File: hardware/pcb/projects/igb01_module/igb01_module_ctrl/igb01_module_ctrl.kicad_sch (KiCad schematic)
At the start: 297 parts, among them J1 ST_JACK_MIDI_OUT, J10 JACK_MAIN_L_OUT, J11 JACK_MAIN_R_OUT, J12 ST_JACK_MIDI_IN, J13 JACK_RST_OUT, J14 JACK_CV2_IN, J15 JACK_CV2_OUT, J16 JACK_CV4_OUT, J17 JACK_CV2_OUT, J18 JACK_CV4_OUT, J19 JACK_RTN_L_IN, J2 JACK_CLK_OUT, J20 JACK_RTN_R_IN, J21 JACK_SND_L_OUT, J22 JACK_SND_R_OUT, J23 TYPE_SELECT, J24 LEFT_CON, J25 RIGHT_CON, J26 TYPE_SELECT, J27 SWD_CON, J28 DISP_CON1, J29 Micro_SD_Card, J3 JACK_CV1_IN, J30 Conn_01x03, J31 Conn_01x03, J32 Conn_01x03, J33 POWER_CON, J4 JACK_CV1_OUT, J5 JACK_CV3_OUT, J6 JACK_CV1_OUT, J7 JACK_CV3_OUT, J8 JACK_EXT_L_IN, J9 JACK_EXT_R_IN, SW1 SW_Push_45deg, SW10 SW_Push_45deg, SW11 SW_Push_45deg, SW12 SW_Push_45deg, SW13 SW_Push_45deg, SW14 SW_Push_45deg, SW15 SW_Push_45deg, SW16 SW_Push_45deg, SW17 SW_Push_45deg, SW18 SW_Push_45deg, SW19 SW_Push_45deg, SW2 SW_Push_45deg, SW20 SW_Push_45deg, SW21 SW_Push_45deg, SW22 SW_Push_45deg, SW23 SW_Push_45deg, SW24 SW_Push_45deg, SW25 SW_Push_45deg, SW26 SW_Push_45deg, SW27 SW_Push_45deg, SW28 SW_Push_45deg, SW29 SW_Push_45deg, SW3 SW_Push_45deg, SW30 SW_Push_45deg, SW31 SW_Push_45deg, SW32 SW_Push_45deg, SW33 SW_Push_45deg, SW34 SW_Push_45deg, SW35 SW_Push_45deg, SW36 SW_Push_45deg, SW4 SW_Push_45deg, SW5 SW_Push_45deg, SW6 SW_Push_45deg, SW7 SW_Push_45deg, SW8 SW_Push_45deg, SW9 SW_Push_45deg, U1 TL074, U10 STM32G431RBTx, U11 TL074, U12 R-78B5.0-2.0, U13 LDK320-3.3V, U14 LDK320-3.3V, U15 LM4040DBZ-10, U2 TL074, U3 74AHCT1G125, U4 TLP2361, U5 74AHCT1G125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

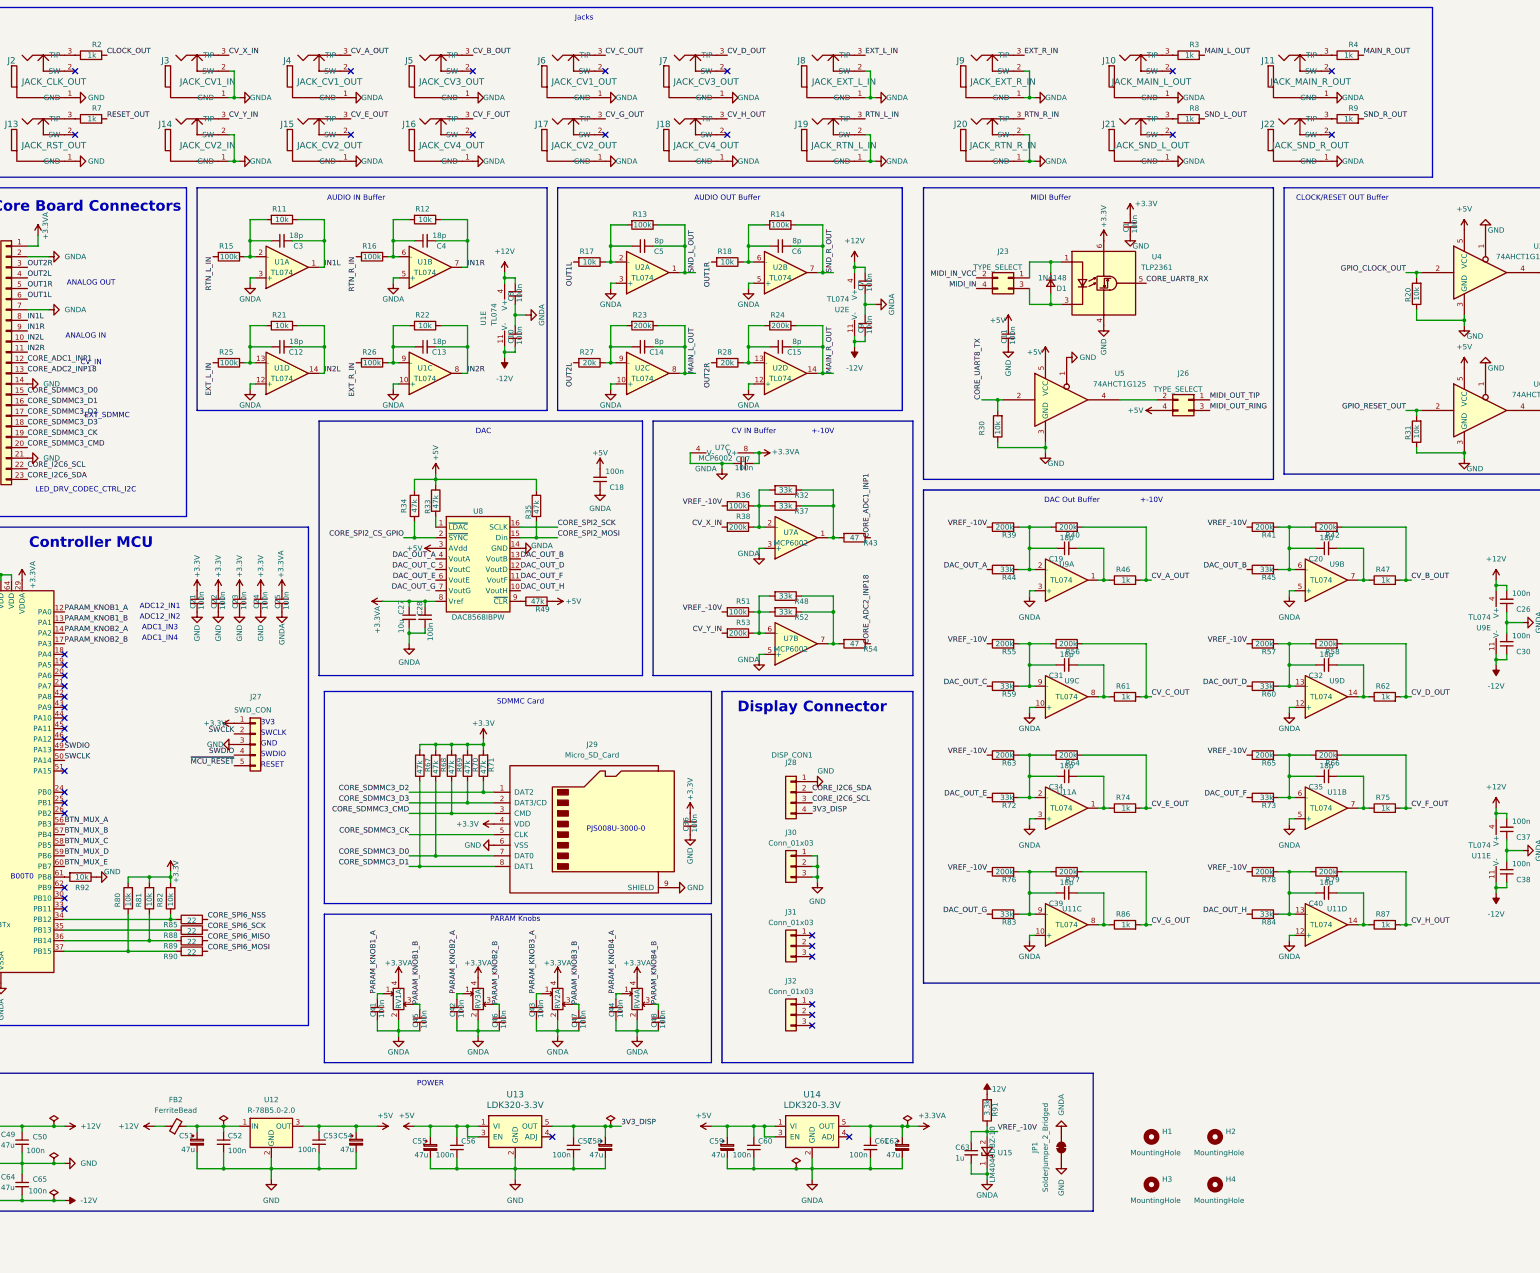
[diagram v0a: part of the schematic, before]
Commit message: update igb01 module control board
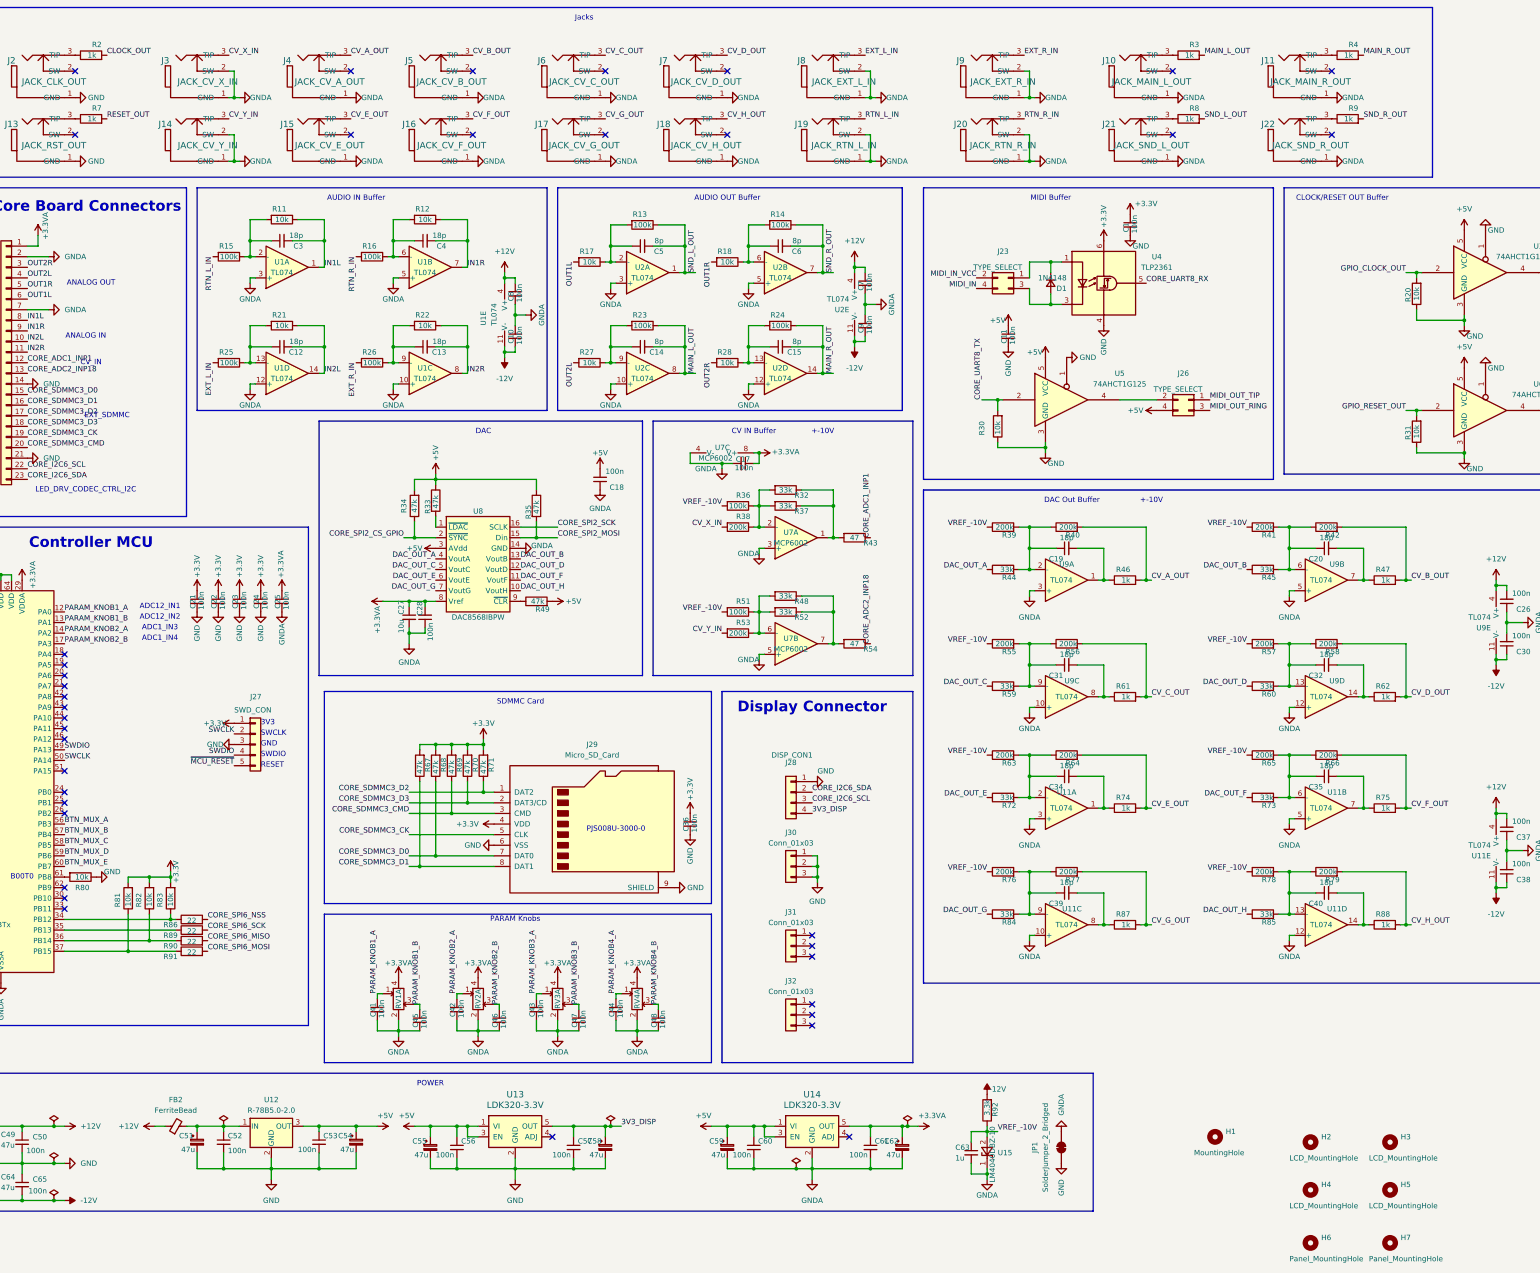
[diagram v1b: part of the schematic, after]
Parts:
- removed H1: MountingHole, MountingHole:MountingHole_3.2mm_M3, symbol Mechanical:MountingHole
- added H2, H5: LCD_MountingHole, MountingHole:MountingHole_2.2mm_M2, symbol Mechanical:MountingHole
- added H6, H7: Panel_MountingHole, MountingHole:MountingHole_3.2mm_M3, symbol Mechanical:MountingHole
- H3, H4: value MountingHole -> LCD_MountingHole; footprint MountingHole:MountingHole_3.2mm_M3 -> MountingHole:MountingHole_2.2mm_M2
- J14: value JACK_CV2_IN -> JACK_CV_Y_IN
- J15: value JACK_CV2_OUT -> JACK_CV_E_OUT
- J16: value JACK_CV4_OUT -> JACK_CV_F_OUT
- J17: value JACK_CV2_OUT -> JACK_CV_G_OUT
- J18: value JACK_CV4_OUT -> JACK_CV_H_OUT
- J3: value JACK_CV1_IN -> JACK_CV_X_IN
- J4: value JACK_CV1_OUT -> JACK_CV_A_OUT
- J5: value JACK_CV3_OUT -> JACK_CV_B_OUT
- J6: value JACK_CV1_OUT -> JACK_CV_C_OUT
- J7: value JACK_CV3_OUT -> JACK_CV_D_OUT
- R23, R24: value 200k -> 100k
- R27, R28: value 20k -> 10k
- renumbered C43 to C42, C42 to C43, C47 to C46, C46 to C47, H2 to H1, R92 to R80, R80 to R81, R81 to R82, R82 to R83, R83 to R84, R84 to R85, R85 to R86, R86 to R87, R87 to R88, R88 to R89, R89 to R90, R90 to R91, R91 to R92
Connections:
- net PARAM_KNOB2_A: now also C42.1, RV2.1; no longer C43.1, RV3.1
- net PARAM_KNOB2_B: now also C46.1, RV2.3; no longer C47.1, RV3.3
- net PARAM_KNOB3_A: now also C43.1, RV3.1; no longer C42.1, RV2.1
- net PARAM_KNOB3_B: now also C47.1, RV3.3; no longer C46.1, RV2.3
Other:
- moved on the sheet: C42, C43, C46, C47, RV2A, RV3A

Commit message: update igb01 module control board
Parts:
- removed C41, C42, C43, C44, C45, C46, C47, C48: 100n, Capacitor_SMD:C_0603_1608Metric, symbol Device:C_Small
- removed R19, R29: 1k, Resistor_SMD:R_0603_1608Metric, symbol Device:R
- removed R32, R48: 33k, Resistor_SMD:R_0603_1608Metric, symbol Device:R
- added C26: 10u, Capacitor_SMD:C_0805_2012Metric, symbol Device:C_Small
- C28: renamed from C27; footprint Capacitor_SMD:C_1206_3216Metric -> Capacitor_SMD:C_0805_2012Metric
- C51: renamed from C58; value 47u -> 100u
- D1: footprint Diode_SMD:D_SOD-323_HandSoldering -> custom:SOD-123
- D10, D11, D12, D13, D14, D15, D16, D17, D18, D19, D2, D20, D21, D22, D23, D24, D25, D26, D27, D28, D29, D3, D30, D31, D32, D33, D34, D35, D36, D37, D38, D39, D4, D40, D41, D5, D6, D7, D8, D9: footprint Diode_SMD:D_SOD-323_HandSoldering -> Diode_SMD:D_SOD-523
- D42, D43: footprint Diode_SMD:D_SOD-123F -> custom:SOD-123
- R1, R10, R5, R6: footprint Resistor_SMD:R_0603_1608Metric -> Resistor_SMD:R_1206_3216Metric
- R2, R3, R4, R7, R8, R9: footprint Resistor_SMD:R_0603_1608Metric -> Resistor_SMD:R_0805_2012Metric
- R30: renamed from R33; footprint Resistor_SMD:R_0402_1005Metric -> Resistor_SMD:R_0603_1608Metric
- R32: renamed from R35; footprint Resistor_SMD:R_0402_1005Metric -> Resistor_SMD:R_0603_1608Metric
- R33: renamed from R36; value 100k -> 200k
- R36: renamed from R39; footprint Resistor_SMD:R_0402_1005Metric -> Resistor_SMD:R_0603_1608Metric
- R37: renamed from R40; footprint Resistor_SMD:R_0402_1005Metric -> Resistor_SMD:R_0603_1608Metric
- R38: renamed from R41; footprint Resistor_SMD:R_0402_1005Metric -> Resistor_SMD:R_0603_1608Metric
- R39: renamed from R42; footprint Resistor_SMD:R_0402_1005Metric -> Resistor_SMD:R_0603_1608Metric
- R41: renamed from R44; footprint Resistor_SMD:R_0402_1005Metric -> Resistor_SMD:R_0603_1608Metric
- R42: renamed from R45; footprint Resistor_SMD:R_0402_1005Metric -> Resistor_SMD:R_0603_1608Metric
- R43: renamed from R46; footprint Resistor_SMD:R_0402_1005Metric -> Resistor_SMD:R_0805_2012Metric
- R44: renamed from R47; footprint Resistor_SMD:R_0402_1005Metric -> Resistor_SMD:R_0805_2012Metric
- R45: renamed from R49; footprint Resistor_SMD:R_0402_1005Metric -> Resistor_SMD:R_0603_1608Metric
- R47: renamed from R51; value 100k -> 200k
- R51: renamed from R55; footprint Resistor_SMD:R_0402_1005Metric -> Resistor_SMD:R_0603_1608Metric
- R52: renamed from R56; footprint Resistor_SMD:R_0402_1005Metric -> Resistor_SMD:R_0603_1608Metric
- R53: renamed from R57; footprint Resistor_SMD:R_0402_1005Metric -> Resistor_SMD:R_0603_1608Metric
- R54: renamed from R58; footprint Resistor_SMD:R_0402_1005Metric -> Resistor_SMD:R_0603_1608Metric
- R55: renamed from R59; footprint Resistor_SMD:R_0402_1005Metric -> Resistor_SMD:R_0603_1608Metric
- R56: renamed from R60; footprint Resistor_SMD:R_0402_1005Metric -> Resistor_SMD:R_0603_1608Metric
- R57: renamed from R61; footprint Resistor_SMD:R_0402_1005Metric -> Resistor_SMD:R_0805_2012Metric
- R58: renamed from R62; footprint Resistor_SMD:R_0402_1005Metric -> Resistor_SMD:R_0805_2012Metric
- R59: renamed from R63; footprint Resistor_SMD:R_0402_1005Metric -> Resistor_SMD:R_0603_1608Metric
- R60: renamed from R64; footprint Resistor_SMD:R_0402_1005Metric -> Resistor_SMD:R_0603_1608Metric
- R61: renamed from R65; footprint Resistor_SMD:R_0402_1005Metric -> Resistor_SMD:R_0603_1608Metric
- R62: renamed from R66; footprint Resistor_SMD:R_0402_1005Metric -> Resistor_SMD:R_0603_1608Metric
- R68: renamed from R72; footprint Resistor_SMD:R_0402_1005Metric -> Resistor_SMD:R_0603_1608Metric
- R69: renamed from R73; footprint Resistor_SMD:R_0402_1005Metric -> Resistor_SMD:R_0603_1608Metric
- R70: renamed from R74; footprint Resistor_SMD:R_0402_1005Metric -> Resistor_SMD:R_0805_2012Metric
- R71: renamed from R75; footprint Resistor_SMD:R_0402_1005Metric -> Resistor_SMD:R_0805_2012Metric
- R72: renamed from R76; footprint Resistor_SMD:R_0402_1005Metric -> Resistor_SMD:R_0603_1608Metric
- R73: renamed from R77; footprint Resistor_SMD:R_0402_1005Metric -> Resistor_SMD:R_0603_1608Metric
- R74: renamed from R78; footprint Resistor_SMD:R_0402_1005Metric -> Resistor_SMD:R_0603_1608Metric
- R75: renamed from R79; footprint Resistor_SMD:R_0402_1005Metric -> Resistor_SMD:R_0603_1608Metric
- R80: renamed from R84; footprint Resistor_SMD:R_0402_1005Metric -> Resistor_SMD:R_0603_1608Metric
- R81: renamed from R85; footprint Resistor_SMD:R_0402_1005Metric -> Resistor_SMD:R_0603_1608Metric
- R83: renamed from R87; footprint Resistor_SMD:R_0402_1005Metric -> Resistor_SMD:R_0805_2012Metric
- R84: renamed from R88; footprint Resistor_SMD:R_0402_1005Metric -> Resistor_SMD:R_0805_2012Metric
- renumbered C26 to C27, C28 to C29, C29 to C30, C30 to C31, C31 to C32, C32 to C33, C33 to C34, C34 to C35, C35 to C36, C36 to C37, C37 to C38, C38 to C39, C39 to C40, C40 to C41, C49 to C42, C50 to C43, C51 to C44, C52 to C45, C53 to C46, C54 to C47, C55 to C48, C56 to C49, C57 to C50, C59 to C52, C60 to C53, C61 to C54, C62 to C55, C63 to C56, C64 to C57, C65 to C58, R20 to R19, R21 to R20, R22 to R21, R23 to R22, R24 to R23, R25 to R24, R26 to R25, R27 to R26, R28 to R27, R30 to R28, R31 to R29, R34 to R31, R37 to R34, R38 to R35, R43 to R40, R50 to R46, R52 to R48, R53 to R49, R54 to R50, R67 to R63, R68 to R64, R69 to R65, R70 to R66, R71 to R67, R80 to R76, R81 to R77, R82 to R78, R83 to R79, R86 to R82, R89 to R85, R90 to R86, R91 to R87, R92 to R88
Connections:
- net +3.3VA: now also C26.1
- net CLOCK_OUT: now also U3.4
- net CV_A_OUT: now also R54.2, R58.2; no longer R37.2, R43.2
- net CV_B_OUT: now also R37.2, R43.2; no longer R39.2, R44.2
- net CV_C_OUT: now also R75.2, R84.2; no longer R52.2, R57.2
- net CV_D_OUT: now also R60.2, R70.2; no longer R54.2, R58.2
- net CV_E_OUT: now also R52.2, R57.2; no longer R60.2, R70.2
- net CV_F_OUT: now also R39.2, R44.2; no longer R62.2, R71.2
- net CV_H_OUT: now also R62.2, R71.2; no longer R75.2, R84.2
- net GNDA: now also C26.2
- net RESET_OUT: now also U6.4

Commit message: update igb01 module control board: layout all nets
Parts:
- removed D2, D3, D4, D5, D6, D7, D8, D9: 1N4148, Diode_SMD:D_SOD-523, symbol Device:D_Small
- removed FB1, FB3: FerriteBead_Small, Resistor_SMD:R_1206_3216Metric, symbol Device:FerriteBead_Small
- removed FB2: FerriteBead, Resistor_SMD:R_1206_3216Metric, symbol Device:FerriteBead_Small
- removed J23, J26: TYPE_SELECT, Connector_PinSocket_2.54mm:PinSocket_2x02_P2.54mm_Vertical, symbol Connector_Generic:Conn_02x02_Odd_Even
- removed JP1: SolderJumper_2_Bridged, custom:GND_JUMPER_no_silk, symbol Jumper:SolderJumper_2_Bridged
- renumbered D18 to D10, D19 to D11, D20 to D12, D21 to D13, D22 to D14, D23 to D15, D24 to D16, D25 to D17, D26 to D18, D27 to D19, D10 to D2, D28 to D20, D29 to D21, D30 to D22, D31 to D23, D32 to D24, D33 to D25, D34 to D26, D35 to D27, D36 to D28, D37 to D29, D11 to D3, D38 to D30, D39 to D31, D40 to D32, D41 to D33, D42 to D34, D43 to D35, D12 to D4, D13 to D5, D14 to D6, D15 to D7, D16 to D8, D17 to D9
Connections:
- net GNDA is gone; now on net GND: C10.1, C16.2, C17.2, C18.1, C2.2, C25.2, C26.2, C27.1, C28.2, C29.1, C31.2, C38.1, C39.2, C52.2, C53.2, C54.2, C55.2, C56.2, C7.2, C8.2, C9.1, J10.1 (GND), J11.1 (GND), J14.1 (GND), J14.2 (SW), J15.1 (GND), J16.1 (GND), J17.1 (GND), J18.1 (GND), J19.1 (GND), J19.2 (SW), J20.1 (GND), J20.2 (SW), J21.1 (GND), J22.1 (GND), J25.2 (Pin_2), J25.7 (Pin_7), J3.1 (GND), J3.2 (SW), J4.1 (GND), J5.1 (GND), J6.1 (GND), J7.1 (GND), J8.1 (GND), J8.2 (SW), J9.1 (GND), J9.2 (SW), RV1.2, RV2.2, RV3.2, RV4.2, U1.10 (+), U1.12 (+), U1.3 (+), U1.5 (+), U10.27 (VSSA), U11.10 (+), U11.12 (+), U11.3 (+), U11.5 (+), U14.2 (GND), U15.1 (K), U2.10 (+), U2.12 (+), U2.3 (+), U2.5 (+), U7.3 (+), U7.4 (V-), U7.5 (+), U8.14 (GND), U9.10 (+), U9.12 (+), U9.3 (+), U9.5 (+)
- net MIDI_OUT_RING is gone; now on net +5V: R5.2
- net +12V: now also C44.1, C45.1, U12.1 (IN)
- net BTN_MUX_1: now also U10.26 (PB2); no longer SW1.2, U10.22 (PC4)
- net BTN_MUX_2: now also U10.25 (PB1); no longer SW2.2, U10.23 (PC5)
- net BTN_MUX_3: now also U10.24 (PB0); no longer SW3.2, U10.38 (PC6)
- net BTN_MUX_4: now also U10.23 (PC5); no longer SW4.2, U10.39 (PC7)
- net BTN_MUX_5: now also U10.22 (PC4); no longer SW5.2, U10.40 (PC8)
- net BTN_MUX_6: now also U10.21 (PA7); no longer SW6.2, U10.41 (PC9)
- net BTN_MUX_7: now also U10.20 (PA6); no longer SW7.2, U10.52 (PC10)
- net BTN_MUX_8: now also U10.19 (PA5); no longer SW8.2, U10.53 (PC11)
- net BTN_MUX_A: now also D2.2 (A), D3.2 (A), D4.2 (A), D5.2 (A), D6.2 (A), D7.2 (A), D8.2 (A), D9.2 (A), U10.46 (PA12); no longer U10.56 (PB3)
- net BTN_MUX_B: now also D10.2 (A), D11.2 (A), D12.2 (A), D13.2 (A), D14.2 (A), D15.2 (A), D16.2 (A), D17.2 (A), U10.45 (PA11); no longer D2.2 (A), D3.2 (A), D4.2 (A), D5.2 (A), D6.2 (A), D7.2 (A), D8.2 (A), D9.2 (A), U10.57 (PB4)
- net BTN_MUX_C: now also D18.2 (A), D19.2 (A), D20.2 (A), D21.2 (A), D22.2 (A), D23.2 (A), D24.2 (A), D25.2 (A), U10.44 (PA10); no longer D10.2 (A), D11.2 (A), D12.2 (A), D13.2 (A), D14.2 (A), D15.2 (A), D16.2 (A), D17.2 (A), U10.58 (PB5)
- net BTN_MUX_D: now also D26.2 (A), D27.2 (A), D28.2 (A), D29.2 (A), D30.2 (A), D31.2 (A), D32.2 (A), D33.2 (A), U10.43 (PA9); no longer D18.2 (A), D19.2 (A), D20.2 (A), D21.2 (A), D22.2 (A), D23.2 (A), D24.2 (A), D25.2 (A), U10.59 (PB6)
- net DAC_OUT_A: now also R56.1; no longer R41.1
- net DAC_OUT_B: now also R81.1; no longer R42.1
- net DAC_OUT_D: now also R80.1; no longer R56.1
- net DAC_OUT_E: now also R42.1; no longer R68.1
- net DAC_OUT_G: now also R41.1; no longer R80.1
- net DAC_OUT_H: now also R68.1; no longer R81.1
- net EXT_L_IN: now also R25.2; no longer R24.2
- net EXT_R_IN: now also R24.2; no longer R25.2
- net GND: now also SW1.2, SW2.2, SW3.2, SW4.2, SW5.2, SW6.2, SW7.2, SW8.2
- net IN1L: now also C4.2, R12.1, U1.7; no longer C3.2, R11.1, U1.1
- net IN1R: now also C3.2, R11.1, U1.1; no longer C4.2, R12.1, U1.7
- net IN2L: now also C13.2, R21.1, U1.8; no longer C12.2, R20.1, U1.14
- net IN2R: now also C12.2, R20.1, U1.14; no longer C13.2, R21.1, U1.8
- net MAIN_L_OUT: now also C15.2, R23.1, U2.14; no longer C14.2, R22.1, U2.8
- net MAIN_R_OUT: now also C5.2, R13.1, U2.1; no longer C15.2, R23.1, U2.14
- net MIDI_IN: now also D1.2 (A), U4.3 (K)
- net MIDI_IN_VCC: now also D1.1 (K), U4.1 (A)
- net MIDI_OUT_TIP: now also U5.4
- net OUT1L: now also R27.2; no longer R17.2
- net OUT1R: now also R17.2; no longer R18.2
- net OUT2R: now also R18.2; no longer R27.2
- net RTN_L_IN: now also R16.2; no longer R15.2
- net RTN_R_IN: now also R15.2; no longer R16.2
- net SND_L_OUT: now also C14.2, R22.1, U2.8; no longer C5.2, R13.1, U2.1
- net C_BTN_8: now reaches SW8.1
- net C_BTN_8: now also U10.53 (PC11)
- net C_BTN_1: now reaches SW1.1
- net C_BTN_1: now also U10.54 (PC12)
- net at J33.1 (Pin_1), J33.2 (Pin_2): now also D35.1 (K)
- net at J33.10 (Pin_10), J33.9 (Pin_9): now also D34.2 (A)
- net C_BTN_7: now reaches SW7.1
- net C_BTN_7: now also U10.52 (PC10)
- net C_BTN_2: now reaches SW2.1
- net C_BTN_2: now also U10.59 (PB6)
- net C_BTN_4: now reaches SW4.1
- net C_BTN_4: now also U10.18 (PA4)
- net C_BTN_6: now reaches SW6.1
- net C_BTN_6: now also U10.33 (PB11)
- net C_BTN_5: now reaches SW5.1
- net C_BTN_5: now also U10.30 (PB10)
- net C_BTN_3: now reaches SW3.1
- net C_BTN_3: now also U10.2 (PC13)
- removed net BTN_MUX_E: D26.2 (A), D27.2 (A), D28.2 (A), D29.2 (A), D30.2 (A), D31.2 (A), D32.2 (A), D33.2 (A), U10.60 (PB7)
- no-connect marks 48 -> 41
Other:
- note added: "Small Buttons"
- moved on the sheet: D10, D11, D12, D13, D14, D15, D16, D17, D18, D19, D2, D20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

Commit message: igb01 module control board ver 0.1
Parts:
- added J23: JTAG, Connector_PinHeader_1.27mm:PinHeader_2x05_P1.27mm_Vertical, symbol Connector_Generic:Conn_02x05_Odd_Even
- H1, H6, H7: footprint MountingHole:MountingHole_3.2mm_M3 -> custom:MountingHole_3.2mm_M3_mod
- H2, H3, H4, H5: footprint MountingHole:MountingHole_2.2mm_M2 -> custom:MountingHole_2.2mm_M2_mod
- J27: footprint Connector_PinHeader_2.54mm:PinHeader_1x05_P2.54mm_Vertical -> Connector_PinSocket_2.54mm:PinSocket_1x05_P2.54mm_Vertical
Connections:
- net +3.3V: now also J23.1 (Pin_1)
- net GND: now also J23.3 (Pin_3), J23.5 (Pin_5), J23.9 (Pin_9)
- net ~{MCU_RESET}: now also J23.10 (Pin_10)
- net JTDI: now reaches U10.51 (PA15)
- net JTDI: now also J23.8 (Pin_8)
- net JTDO-TRACESWO: now reaches U10.56 (PB3)
- net JTDO-TRACESWO: now also J23.6 (Pin_6)
- net SWCLK renamed JTCK-SWCLK
- net JTCK-SWCLK: now also J23.4 (Pin_4)
- net SWDIO renamed JTMS-SWDIO
- net JTMS-SWDIO: now also J23.2 (Pin_2)
- no-connect marks 41 -> 40
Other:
- moved on the sheet: J27
